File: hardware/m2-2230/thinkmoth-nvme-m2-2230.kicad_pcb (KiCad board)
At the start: 2 copper layers, 31 x 55.9 mm, 18 parts, among them J2 ExpressCard, J3 MDT180M03001, U1 GL823K-HCY04

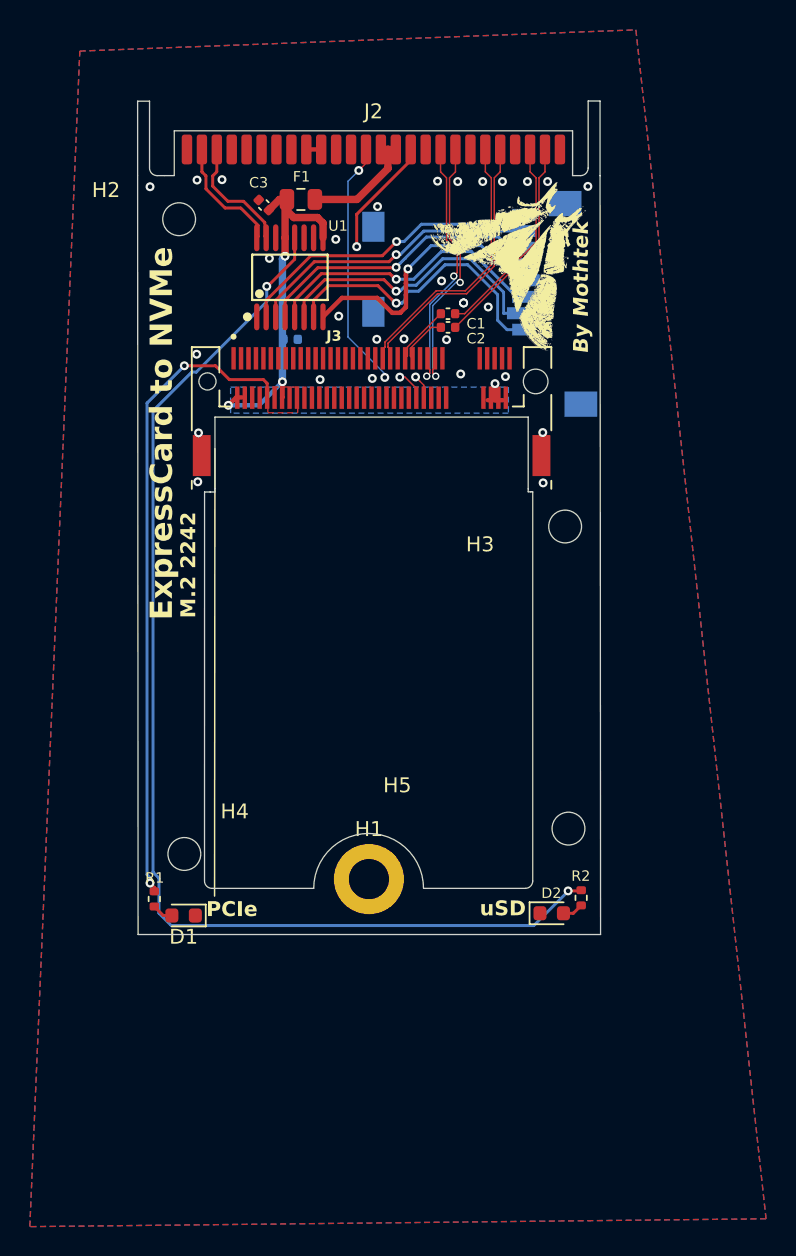
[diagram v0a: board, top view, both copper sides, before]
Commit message: keeping legacy m.2 2230 design around... for now
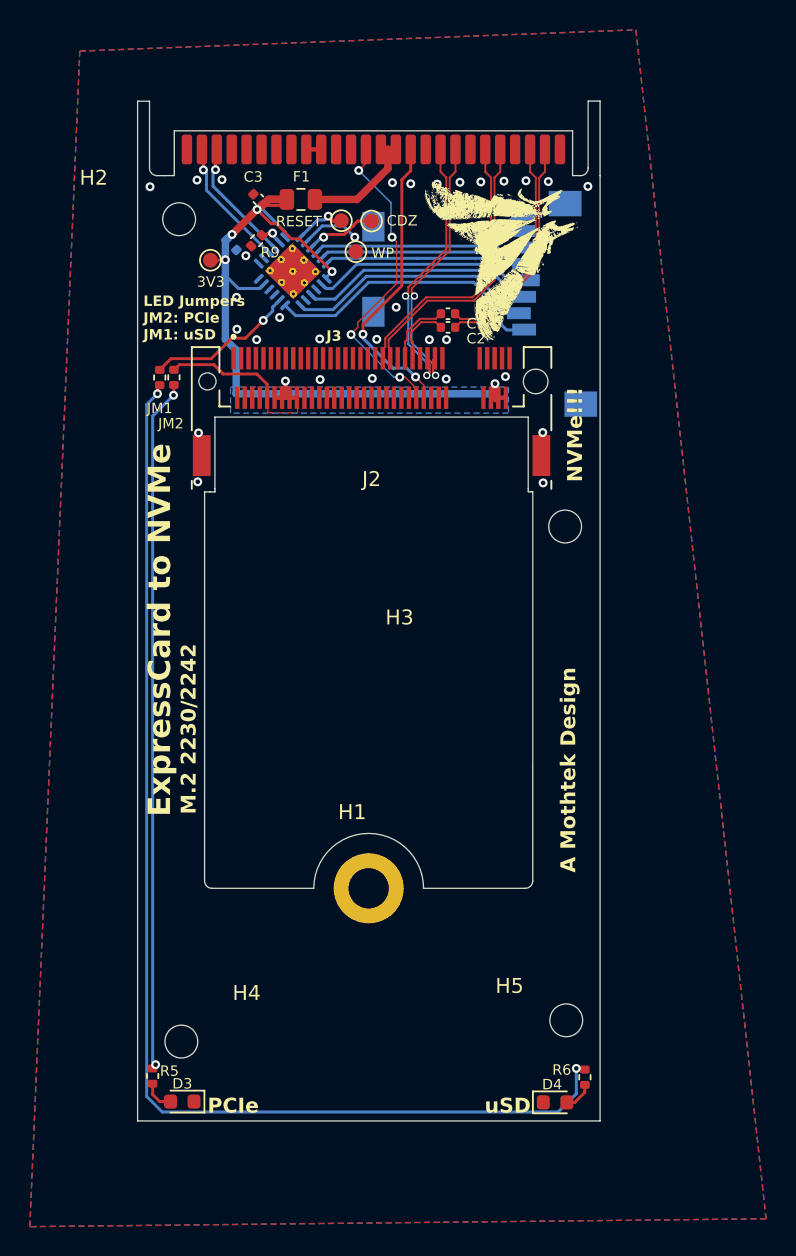
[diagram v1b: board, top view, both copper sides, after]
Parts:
- removed D1, D2: LED, LED_SMD:LED_0603_1608Metric
- removed R1, R2: 680r, Resistor_SMD:R_0402_1005Metric
- removed U1: GL823K-HCY04, GL823K-HCY04:SSOP-16_L4.9-W3.9-P0.64-LS6.0-BL
- added 3V3: 3V3, TestPoint:TestPoint_Pad_D1.0mm, F.Cu at (65.1, 59.9)
- added CDZ: SD_CDZ, TestPoint:TestPoint_Pad_D1.0mm, F.Cu at (75.9, 57.3)
- added D3: LED, LED_SMD:LED_0603_1608Metric, F.Cu at (63.2, 116.3)
- added D4: LED, LED_SMD:LED_0603_1608Metric, F.Cu at (88.2, 116.4)
- added JM1: 0r, Resistor_SMD:R_0402_1005Metric, F.Cu at (61.7, 67.8)
- added JM2: 0r, Resistor_SMD:R_0402_1005Metric, F.Cu at (62.6, 67.8)
- added R5: 4kR, Resistor_SMD:R_0402_1005Metric, F.Cu at (61.2, 114.6)
- added R6: 4kR, Resistor_SMD:R_0402_1005Metric, F.Cu at (90.2, 114.7)
- added R9: 680r, Resistor_SMD:R_0402_1005Metric, F.Cu at (68.2, 58.6)
- added RESET: SD_RESET, TestPoint:TestPoint_Pad_D1.0mm, F.Cu at (73.8, 57.3)
- added U2: ~, Package_DFN_QFN:QFN-24-1EP_4x4mm_P0.5mm_EP2.7x2.6mm_ThermalVias, B.Cu at (70.6, 60.7)
- added WP: SD_WP, TestPoint:TestPoint_Pad_D1.0mm, F.Cu at (74.8, 59.4)
- moved H5 12.9 mm to (88.9, 110.9)
- moved H4 12.6 mm to (63.1, 112.3)
- moved C4 7.47 mm to (66.5, 58.9), turned to 135 degrees
- moved H1 0.62 mm to (75.7, 102.0)
- moved C3 0.53 mm to (68.3, 55.8)
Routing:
- net Net-(JM1-Pad1): track 0.00 -> 80.1 mm, vias 0 -> 2
- net SD_LED: track 79.2 -> 10.1 mm, vias 2 -> 1
- net Net-(JM2-Pad1): track 0.00 -> 46.6 mm, vias 0 -> 2
- net PCIe_LED: track 43.5 -> 7.82 mm, vias 2 -> 0
- net 3V3: track 28.1 -> 57.3 mm, vias 4 -> 6
- net CLKREQ: track 9.63 -> 20.2 mm
- net SD_CLK: track 20.2 -> 13.5 mm, vias 1 -> 0
- net SD_DAT1: track 20.8 -> 14.8 mm, vias 1 -> 0
- net SD_DAT0: track 19.7 -> 14.3 mm, vias 1 -> 0
- net SD_CDZ: track 0.00 -> 4.81 mm, vias 0 -> 1
- net SD_WP: track 0.00 -> 4.18 mm, vias 0 -> 1
- net SD_3V3: track 18.9 -> 15.1 mm, vias 1 -> 0
- net SD_RESET: track 0.00 -> 3.49 mm, vias 0 -> 1
- net SD_CMD: track 19.4 -> 15.9 mm, vias 1 -> 0
- net SD_DAT3: track 19.6 -> 16.7 mm, vias 1 -> 0
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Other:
- board size 31 x 55.9 mm -> 31 x 68.4 mm
- board text added: "A Mothtek Design"
- board text added: "LED Jumpers JM2: PCIe JM1: uSD"
- board text added: "M.2 2230/2242"
- board text added: "Moth"
- board text added: "NVMe!!!"
- board text added: "Think"
- board text removed: "By Mothtek"
- board text removed: "M.2 2242"
- board text removed: "ThinkMoth"
